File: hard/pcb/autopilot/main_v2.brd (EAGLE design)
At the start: 100 x 65 mm, 168 parts, among them IC1 24AA32ASN, IC2 INA194, IC3 LP2950Z, Q1 IRLML5203, Q3 IRLML5203, Q4 IRLML5203, T3 BC848, U2 TMP75DGK, U44 BMP085, X1 USB-SMD-NS

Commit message: Changed in PCB
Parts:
- moved C45 205.1 mm to (72.0, 6.00), flipped to the bottom, turned to 180 degrees
- moved R36 201.5 mm to (69.0, 4.00), flipped to the bottom, turned to 90 degrees
- moved DA6 195.2 mm to (86.3, 6.91), flipped to the bottom, turned to 90 degrees
- moved IC2 194.8 mm to (72.3, 9.52), flipped to the bottom, turned to 270 degrees
- moved R9 191.8 mm to (66.0, 26.0), flipped to the bottom
- moved DA4 182.8 mm to (72.9, 21.7), flipped to the bottom
- moved C49 182.3 mm to (72.2, 17.3), flipped to the bottom
- moved XP18 179.7 mm to (71.0, 3.00)
- moved DA2 178.0 mm to (80.3, 11.2), turned to 90 degrees
- moved R51 168.6 mm to (76.0, 4.00), flipped to the bottom, turned to 90 degrees
- moved DD3 160.9 mm to (79.5, 45.0), flipped to the bottom, turned to 180 degrees
- moved XP6 156.9 mm to (47.0, 3.00), turned to 90 degrees
- moved L1 153.2 mm to (93.7, 28.9), flipped to the bottom, turned to 270 degrees
- moved XP16 150.5 mm to (50.0, 3.00), turned to 90 degrees
- moved U44 149.8 mm to (18.5, 4.33), flipped to the bottom
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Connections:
- removed net N$12: C14.A, C15.1, DA4.1, DA4.3, L1.2
- new net N$30: C14.A, C15.1, DA4.1, DA4.3, L1.2, Q1.2, R59.1
- net 6V: no longer Q1.2, R59.1
- net I2C_FAST_SCL: now also DD1.92; no longer DD1.47
- net I2C_FAST_SDA: now also DD1.93; no longer DD1.48
- net I2C_SLOW_SCL: now also DD1.47; no longer DD1.92
- net I2C_SLOW_SDA: now also DD1.48; no longer DD1.93
- net MPXV_TEMP: now also DD1.17; no longer DD1.33
- net N$54: now also DD1.33; no longer DD1.17
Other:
- board size 100 x 65 mm -> 102 x 67 mm
- board text added: "TODO: change package for microsd change crystals to SMD change aluminium capacitors to tantalum cnage analog inductor to ferrite bead add keepoout to adis's mounting holes move LSM303 to fast i2c bus change SM6T12 to something for 6..7v meeling in board for pressure connector"

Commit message: NOP
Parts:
- removed C43: 0.1uF, SparkFun:0805
- removed R53: 2.2, barthess:R1206
- removed R6: 330, SparkFun:0805
- added C41: 10uF, SparkFun:1206
- added C42: 0.1uF, SparkFun:0805
- C31: value 330uF/16v -> 330uF/10v; device SparkFun:CPOL-RADIAL-1000UF-25V -> barthess:EIA7343
- C34: value 560uF/4v -> 470uF/6.3v; device rcl:E3,5-8 -> barthess:EIA7343
- L1: device SparkFun:1210 -> ferrite:L0603
- ZQ1: device barthess:HC49U-V -> crystal:CRYSTAL-SMD-5X3
- ZQ2: device barthess:TC38H -> crystal:CRYSTAL-32KHZ-SMD-3.2X1.5
- moved Q1 214.1 mm to (95.0, 28.0), flipped to the bottom, turned to 90 degrees
- moved C24 208.4 mm to (89.0, 15.8), flipped to the bottom
- moved R33 206.4 mm to (84.0, 12.0), flipped to the bottom, turned to 270 degrees
- moved C14 194.4 mm to (66.0, 14.0), flipped to the bottom, turned to 180 degrees
- moved R61 184.1 mm to (86.2, 31.0), flipped to the bottom
- moved R59 183.4 mm to (93.0, 31.0), flipped to the bottom
- moved C55 181.0 mm to (95.0, 25.0), flipped to the bottom
- moved R58 180.8 mm to (92.0, 28.0), flipped to the bottom, turned to 270 degrees
- moved C17 177.0 mm to (76.2, 11.2), flipped to the bottom, turned to 90 degrees
- moved C34 170.0 mm to (83.7, 58.9), flipped to the bottom, turned to 90 degrees
- moved C50 168.6 mm to (86.0, 22.0), flipped to the bottom
- moved R48 163.1 mm to (83.2, 15.5), flipped to the bottom, turned to 90 degrees
- moved R47 161.9 mm to (85.8, 15.8), flipped to the bottom
- moved R45 161.7 mm to (88.0, 10.5), flipped to the bottom
- moved C16 159.9 mm to (66.0, 21.0), flipped to the bottom, turned to 270 degrees
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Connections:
- removed net N$38: C43.1, R53.1
- removed net N$8: C12.2, R6.1, ZQ1.2
- net +3.3V_A: now also C41.1, DA6.7; no longer R53.2
- net 3.3V: now also C34.A; no longer C34.+, DA6.7
- net 6V: now also C31.A, C42.1; no longer C31.1
- net GND: now also C31.C, C34.C, C42.2; no longer C31.2, C34.-
- net GND_A: now also C41.2; no longer C43.2
- net I2C_FAST_SCL: now also DD5.2
- net I2C_FAST_SDA: now also DD5.3
- net I2C_SLOW_SCL: no longer DD5.2
- net I2C_SLOW_SDA: no longer DD5.3
- net N$1: now also ZQ2.P$2; no longer ZQ2.2
- net N$6: now also ZQ2.P$1; no longer ZQ2.1
- net N$7: now also C12.2, ZQ1.3; no longer R6.2
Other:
- outline, holes or cut-outs redrawn
- board text added: "TODO: check ferrite bead fiducial marks"
- board text removed: "TODO: change package for microsd change crystals to SMD change aluminium capacitors to tantalum cnage analog inductor to ferrite bead add keepoout to adis's mounting holes move LSM303 to fast i2c bus change SM6T12 to something for 6..7v meeling in board for pressure connector"

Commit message: Board v2
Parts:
- moved R10 214.0 mm to (77.0, 7.00), flipped to the bottom
- moved C28 203.5 mm to (90.0, 78.0), turned to 270 degrees
- moved C25 201.7 mm to (99.0, 75.0)
- moved C26 200.3 mm to (93.2, 72.5)
- moved C33 187.3 mm to (80.0, 74.0), flipped to the bottom, turned to 90 degrees
- moved R31 182.1 mm to (60.0, 9.00), turned to 90 degrees
- moved C18 180.7 mm to (76.0, 10.0), flipped to the bottom, turned to 90 degrees
- moved C19 178.9 mm to (99.0, 77.0), turned to 180 degrees
- moved R30 177.5 mm to (58.0, 9.00), turned to 90 degrees
- moved U$7 174.0 mm to (58.5, 4.68)
- moved C7 171.4 mm to (40.0, 10.0), flipped to the bottom, turned to 90 degrees
- moved R60 169.9 mm to (56.0, 9.00), turned to 90 degrees
- moved R56 167.4 mm to (64.0, 5.00), flipped to the bottom
- moved R54 163.7 mm to (64.0, 3.00), flipped to the bottom, turned to 180 degrees
- moved C22 158.9 mm to (68.0, 81.0)
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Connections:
- removed net N$33: R60.1, U$7.G
- removed net N$57: R30.1, U$7.R
- new net N$12: R60.1, U$7.R
- new net N$8: R30.1, U$7.G
- net CURRENT_SENS: now also DD1.17; no longer DD1.15
- net MPXV_TEMP: now also DD1.16; no longer DD1.17
- net N$52: now also DD1.18; no longer DD1.16
- net PRESS_DIFF: now also DD1.15; no longer DD1.18
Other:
- board text added: "TODO: check ferrite bead fiducial marks add restricted area under adis"
- board text removed: "TODO: check ferrite bead fiducial marks"

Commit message: board v2 nop
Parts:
- moved C29 217.5 mm to (99.3, 72.0), turned to 180 degrees
- moved C51 216.6 mm to (86.5, 26.3), flipped to the bottom, turned to 90 degrees
- moved R8 198.7 mm to (85.0, 42.0), flipped to the bottom, turned to 90 degrees
- moved R29 190.6 mm to (96.0, 39.0), flipped to the bottom
- moved C54 171.9 mm to (90.0, 28.0), flipped to the bottom, turned to 90 degrees
- moved C6 171.5 mm to (68.0, 40.0), flipped to the bottom
- moved R28 166.9 mm to (86.0, 68.0), flipped to the bottom, turned to 180 degrees
- moved R32 164.5 mm to (60.6, 49.4), flipped to the bottom, turned to 90 degrees
- moved R27 162.7 mm to (86.0, 70.0), flipped to the bottom, turned to 180 degrees
- moved R11 158.3 mm to (9.00, 13.0), flipped to the bottom
- moved F3 156.9 mm to (57.0, 63.0), flipped to the bottom, turned to 180 degrees
- moved R37 156.6 mm to (34.0, 38.0), flipped to the bottom, turned to 180 degrees
- moved C27 155.0 mm to (15.0, 17.0), flipped to the bottom
- moved D3 153.1 mm to (59.0, 58.0), flipped to the bottom, turned to 270 degrees
- moved C23 152.6 mm to (48.0, 51.0), flipped to the bottom, turned to 225 degrees
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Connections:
- new net N$33: C40.1, DD1.6, VD4.3
- net 3.3V: no longer C40.1, DD1.6, VD4.3

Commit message: board v2. nop
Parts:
- removed C49: 2.2uF, rcl:C1206
- added C43: 2.2uF, SparkFun:0805
- moved JP6 41.7 mm to (27.4, 73.3), flipped to the bottom, turned to 90 degrees
- moved R26 34.4 mm to (39.0, 70.0)
- moved R37 34.4 mm to (39.0, 72.0)
- moved C41 16.8 mm to (83.0, 23.5), turned to 90 degrees
- moved C51 8.10 mm to (94.5, 27.6)
- moved C22 6.79 mm to (72.2, 13.8)
- moved C37 6.79 mm to (70.8, 7.75)
- moved C45 6.79 mm to (75.0, 9.75)
- moved IC2 6.79 mm to (75.1, 13.3)
- moved R36 6.79 mm to (73.5, 6.75)
- moved R51 6.79 mm to (76.2, 6.75)
- moved R54 6.79 mm to (70.8, 3.75)
- moved R56 6.79 mm to (70.8, 5.75)
- moved VD2 6.79 mm to (70.2, 11.8)
- moved XP18 6.79 mm to (73.8, 3.75)
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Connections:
- net GND_A: now also C43.2; no longer C49.1
- net N$47: now also C43.1; no longer C49.2
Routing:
- net GND_A: track 0.00 -> 105.7 mm, vias 0 -> 4
- net +3.3V_A: track 0.00 -> 37.0 mm
- net N$30: track 0.00 -> 33.3 mm, vias 0 -> 2
- net +5V_A: track 0.00 -> 30.7 mm, vias 0 -> 1
- net N$55: track 0.00 -> 18.1 mm, vias 0 -> 1
- net N$52: track 0.00 -> 10.8 mm
- net MAIN_SUPPLY: track 0.00 -> 8.12 mm
- net NET$1: track 0.00 -> 6.51 mm
- net N$46: track 0.00 -> 5.89 mm
- net N$47: track 0.00 -> 5.86 mm
- net N$11: track 0.00 -> 5.68 mm
- net N$20: track 0.00 -> 4.78 mm
- net N$37: track 0.00 -> 4.74 mm
- net N$53: track 0.00 -> 4.25 mm
- net N$15: track 0.00 -> 4.20 mm
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
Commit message: board v2 nop
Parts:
- removed R9: 0, SparkFun:0805
- added R6: 0, barthess:R1206
- moved ZQ2 2.18 mm to (65.9, 32.5)
- moved C10 2.10 mm to (69.0, 31.4), turned to 225 degrees
- moved ZQ1 1.79 mm to (63.6, 27.8)
- moved C12 1.63 mm to (66.6, 24.9)
- moved C3 1.55 mm to (57.0, 27.9), turned to 270 degrees
- moved C11 1.38 mm to (66.4, 28.9)
- moved C9 1.38 mm to (67.6, 30.1), turned to 225 degrees
- moved C5 0.88 mm to (62.6, 32.4)
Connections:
- net GND: now also R6.2; no longer R9.1
- net GND_A: now also R6.1; no longer R9.2
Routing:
- net PRESS_DIFF: track 2.52 -> 46.4 mm, vias 0 -> 2
- net CURRENT_SENS: track 0.00 -> 34.4 mm, vias 0 -> 2
- net GND_A: track 105.7 -> 136.8 mm, vias 4 -> 5
- net +3.3V_A: track 37.0 -> 67.7 mm, vias 0 -> 2
- net MPXV_TEMP: track 3.26 -> 32.2 mm, vias 0 -> 1
- net 3.3V: track 0.00 -> 13.9 mm
- net N$7: track 0.00 -> 11.0 mm
- net N$9: track 0.00 -> 9.66 mm
- net N$6: track 0.00 -> 9.64 mm
- net N$1: track 0.00 -> 9.47 mm
- net GND: track 0.00 -> 8.29 mm
- net N$52: track 10.8 -> 15.1 mm
- net N$82: track 0.00 -> 2.48 mm
- net +5V_A: track 30.7 -> 33.1 mm
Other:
- outline, holes or cut-outs redrawn

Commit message: board v2 nop
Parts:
- removed C51: 10uF/16v, SparkFun:EIA3216-KIT
- added F1: POLYSWITCH, barthess:1812
- moved R55 45.1 mm to (75.0, 27.8), turned to 90 degrees
- moved R57 42.5 mm to (73.2, 27.8), turned to 90 degrees
- moved VD3 40.7 mm to (71.4, 23.4), turned to 270 degrees
- moved C39 39.8 mm to (71.4, 27.8), turned to 90 degrees
- moved XP17 24.0 mm to (34.0, 59.0)
- moved L1 16.8 mm to (79.7, 29.7)
- moved R32 9.98 mm to (67.0, 41.6), turned to 135 degrees
- moved C7 7.09 mm to (37.4, 3.40), turned to 0 degrees
- moved Q3 6.65 mm to (32.2, 3.40)
- moved R15 6.61 mm to (29.6, 3.40)
- moved C44 5.06 mm to (41.8, 41.0), turned to 225 degrees
- moved C8 4.68 mm to (34.4, 5.60)
- moved C34 4.53 mm to (85.2, 52.4)
- moved XP10 3.00 mm to (16.0, 59.0)
- moved XP11 3.00 mm to (19.0, 59.0)
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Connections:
- new net N$36: D2.C, F1.1
- net 6V: now also F1.2; no longer D2.C
- net GND_A: no longer C51.C
- net N$55: no longer C51.A
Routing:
- net 6V: track 0.00 -> 140.3 mm, vias 0 -> 6
- net TO_XBEE: track 0.00 -> 64.2 mm, vias 0 -> 3
- net FROM_XBEE: track 0.00 -> 63.9 mm, vias 0 -> 2
- net GND: track 8.29 -> 71.3 mm, vias 0 -> 2
- net XBEE_CTS: track 0.00 -> 62.4 mm, vias 0 -> 2
- net FROM_GPS: track 0.00 -> 59.8 mm, vias 0 -> 4
- net TO_GPS: track 0.00 -> 59.7 mm, vias 0 -> 3
- net 3.3V: track 13.9 -> 70.2 mm, vias 0 -> 1
- net SDIO_D2: track 0.00 -> 54.0 mm, vias 0 -> 1
- net GPS_ENABLE: track 0.00 -> 53.4 mm, vias 0 -> 1
- net SDIO_CMD: track 0.00 -> 52.4 mm, vias 0 -> 1
- net SDIO_D3: track 0.00 -> 51.9 mm, vias 0 -> 1
- net RECEIVER_PPM: track 0.00 -> 51.6 mm, vias 0 -> 4
- net SDIO_CK: track 0.00 -> 50.3 mm, vias 0 -> 1
- net GPS_PPS: track 0.00 -> 48.8 mm, vias 0 -> 4
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- added copper zone on layer 16, net 3.3V
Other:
- board text added: "TODO: fiducial marks add restricted area under adis fix adis silk screen >NAME and >VALUE"
- board text removed: "TODO: check ferrite bead fiducial marks add restricted area under adis"

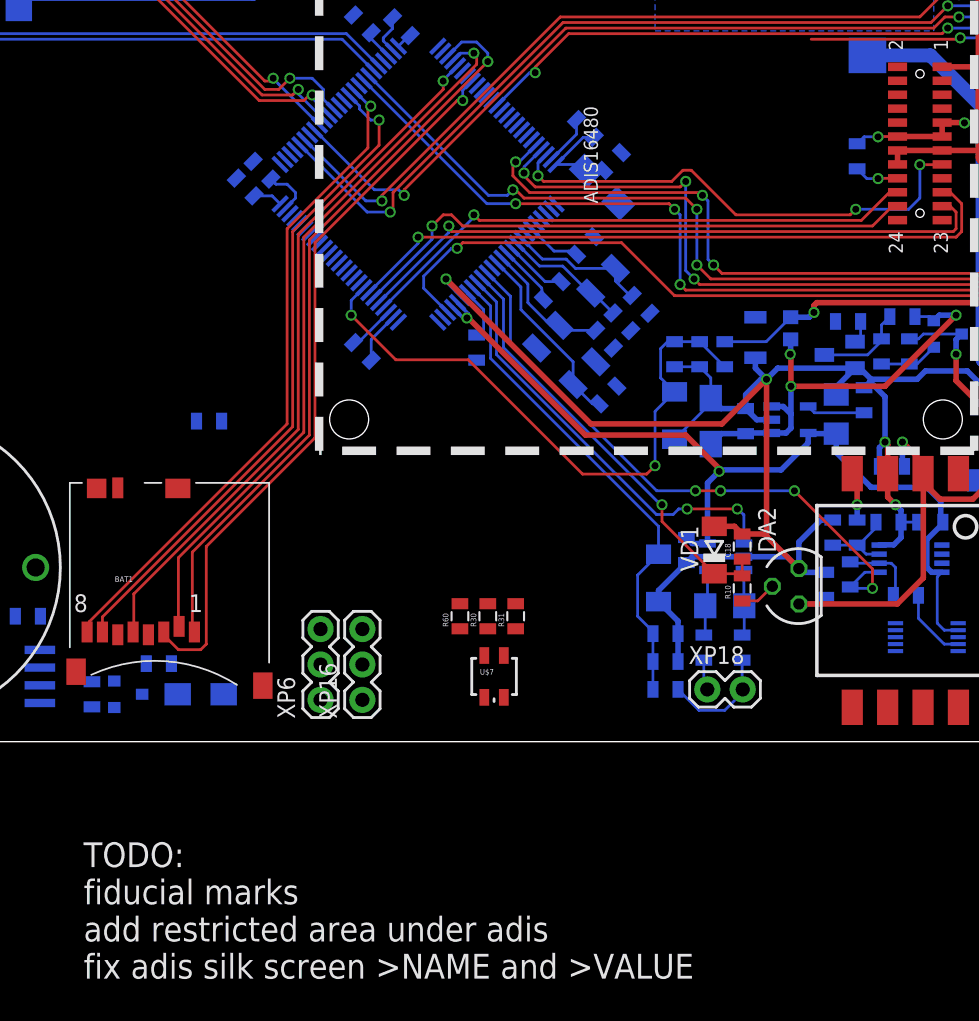
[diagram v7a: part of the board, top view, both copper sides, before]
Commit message: board v2. Minor fixes
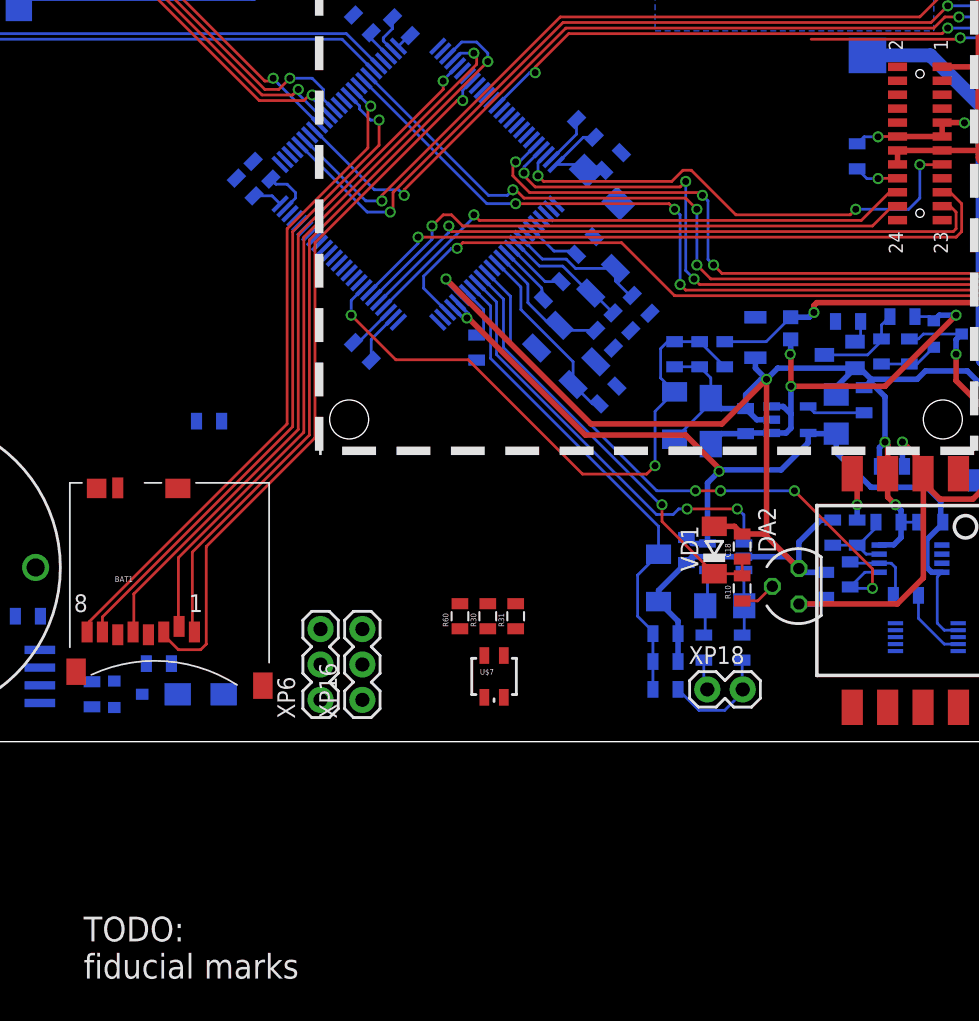
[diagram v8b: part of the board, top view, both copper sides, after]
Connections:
- net N$1: now also ZQ2.2; no longer ZQ2.P$2
- net N$6: now also ZQ2.1; no longer ZQ2.P$1
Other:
- board text added: "TODO: fiducial marks"
- board text removed: "TODO: fiducial marks add restricted area under adis fix adis silk screen >NAME and >VALUE"
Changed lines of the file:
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@@
 <wire x1="0" y1="67" x2="0" y2="0" width="0" layer="20"/>
 <text x="29" y="-17" size="1.778" layer="21">TODO:
-fiducial marks
-add restricted area under adis
-fix adis silk screen &gt;NAME and &gt;VALUE</text>
+fiducial marks</text>
 <wire x1="102" y1="20" x2="99" y2="17" width="0" layer="20"/>
 <wire x1="99" y1="17" x2="94" y2="17" width="0" layer="20"/>
@@
 <signal name="N$1">
 <contactref element="C9" pad="1"/>
-<contactref element="ZQ2" pad="P$2"/>
+<contactref element="ZQ2" pad="2"/>
 <contactref element="DD1" pad="9"/>
 <wire x1="60.07106875" y1="35.75735625" x2="61.703425" y2="34.125" width="0.2" layer="16"/>
@@
 <signal name="N$6">
 <contactref element="C10" pad="1"/>
-<contactref element="ZQ2" pad="P$1"/>
+<contactref element="ZQ2" pad="1"/>
 <contactref element="DD1" pad="8"/>
 <wire x1="60.424621875" y1="36.1109125" x2="61.910534375" y2="34.625" width="0.2" layer="16"/>
